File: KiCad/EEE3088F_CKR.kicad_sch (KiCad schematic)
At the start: 0 parts

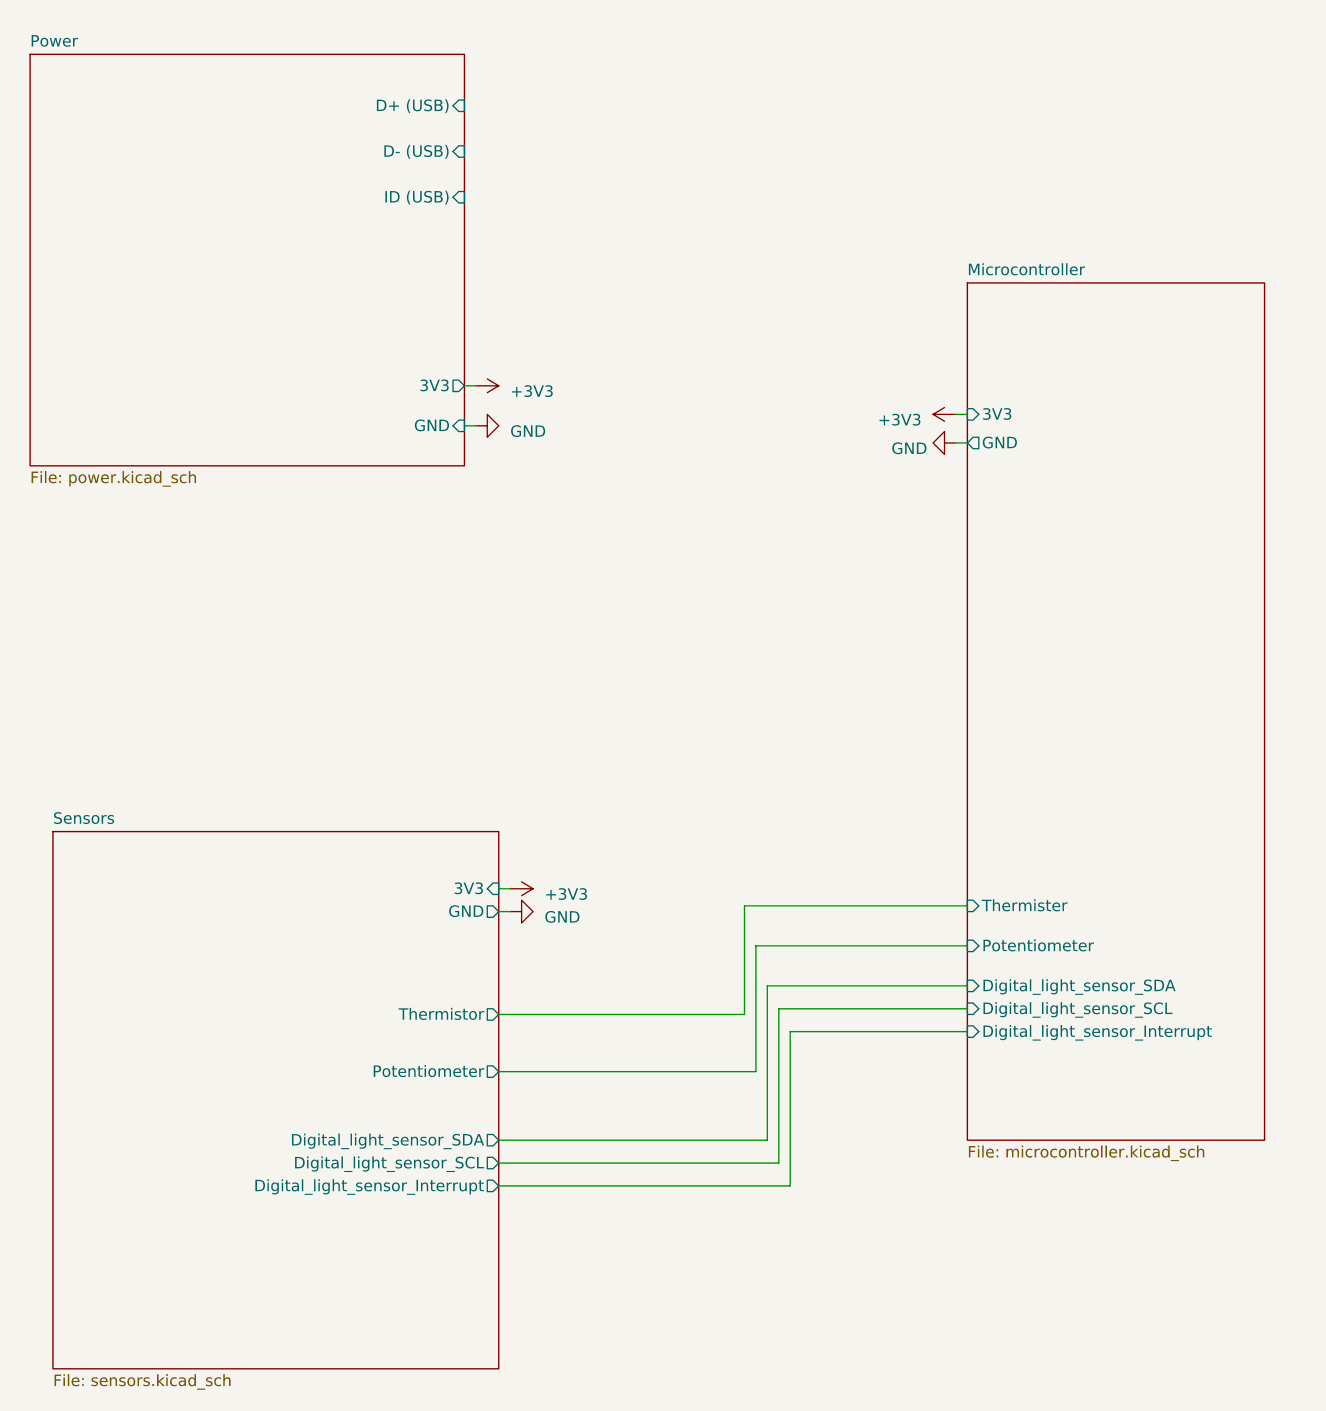
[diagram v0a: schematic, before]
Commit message: added USB to UART connector and made a dedicated USB sheet
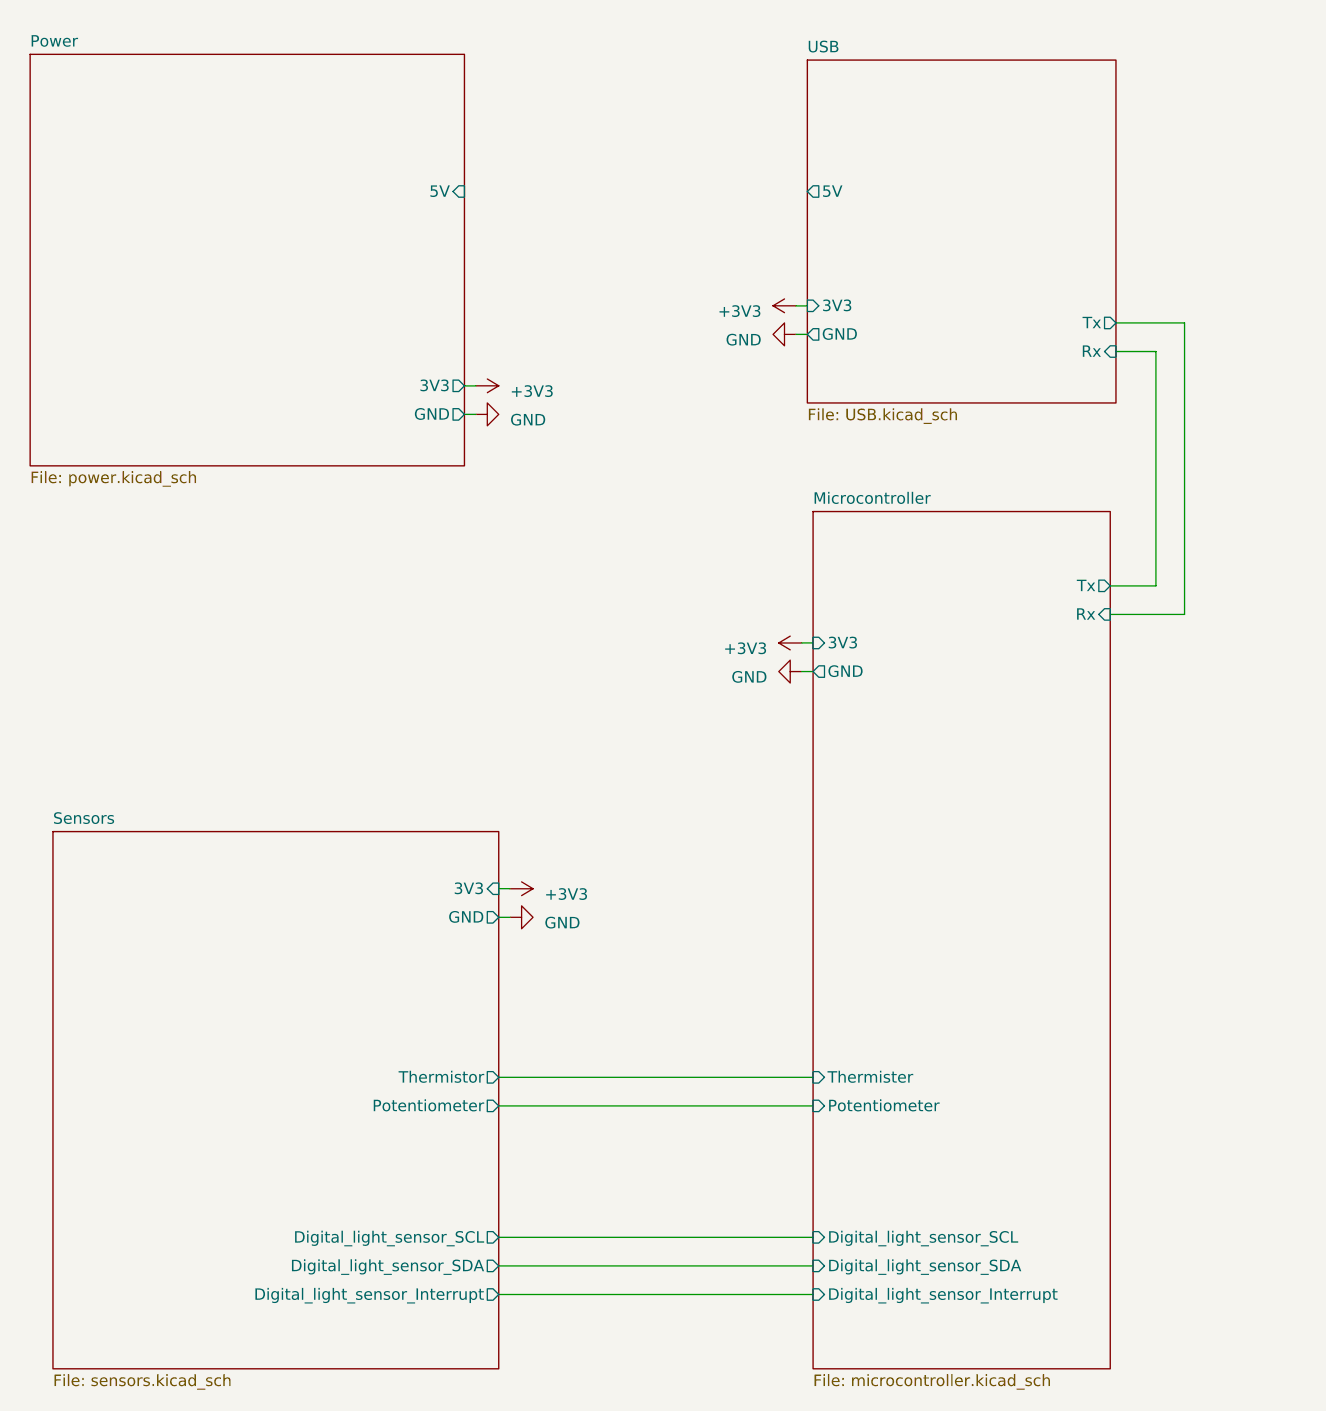
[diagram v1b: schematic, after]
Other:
- added sheet USB (USB.kicad_sch)
- sheet Microcontroller ports: added Rx, Tx; removed none
- sheet Power ports: added 5V; removed D+ (USB), D- (USB), ID (USB)

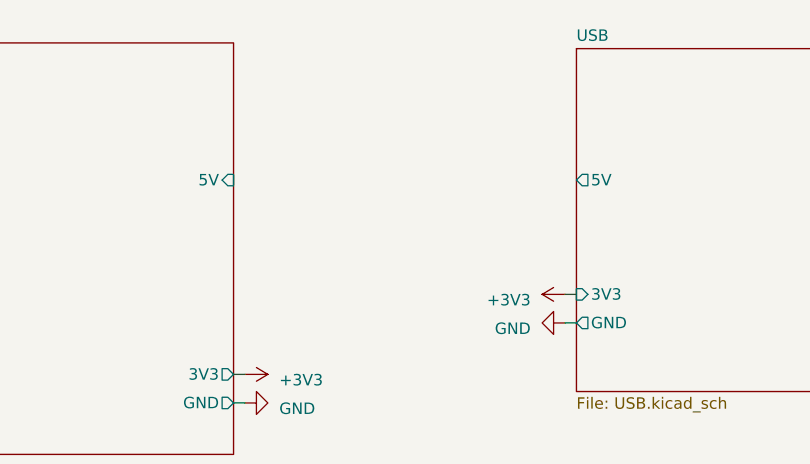
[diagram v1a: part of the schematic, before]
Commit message: Added sheet notes and initial design template, reordered microcontoller subsheet and add microntoller subsheet notes
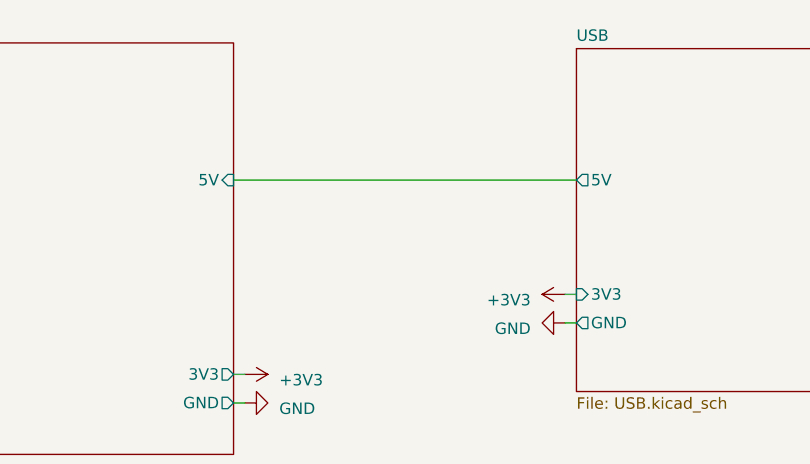
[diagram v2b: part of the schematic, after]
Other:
- company: (none) -> UCT
- title: (none) -> Root
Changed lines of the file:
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@@
 (kicad_sch (version 20230121) (generator eeschema)
   (paper "A4")
+  (title_block
+    (title "Root")
+    (date "2023-03-11")
+    (rev "v0.3")
+    (company "UCT")
+    (comment 1 "Authors: Cameron Clark, Robert Dugmore, Kian Frassek")
+    (comment 2 "This is an overview sheet showing how the sub-circuits interconnect")
+  )
   (wire (pts (xy 118.11 55.88) (xy 116.84 55.88))
     (stroke (width 0) (type default))
@@
     (stroke (width 0) (type default))
   )
+  (wire (pts (xy 80.01 43.18) (xy 118.11 43.18))
+    (stroke (width 0) (type default))
+  )

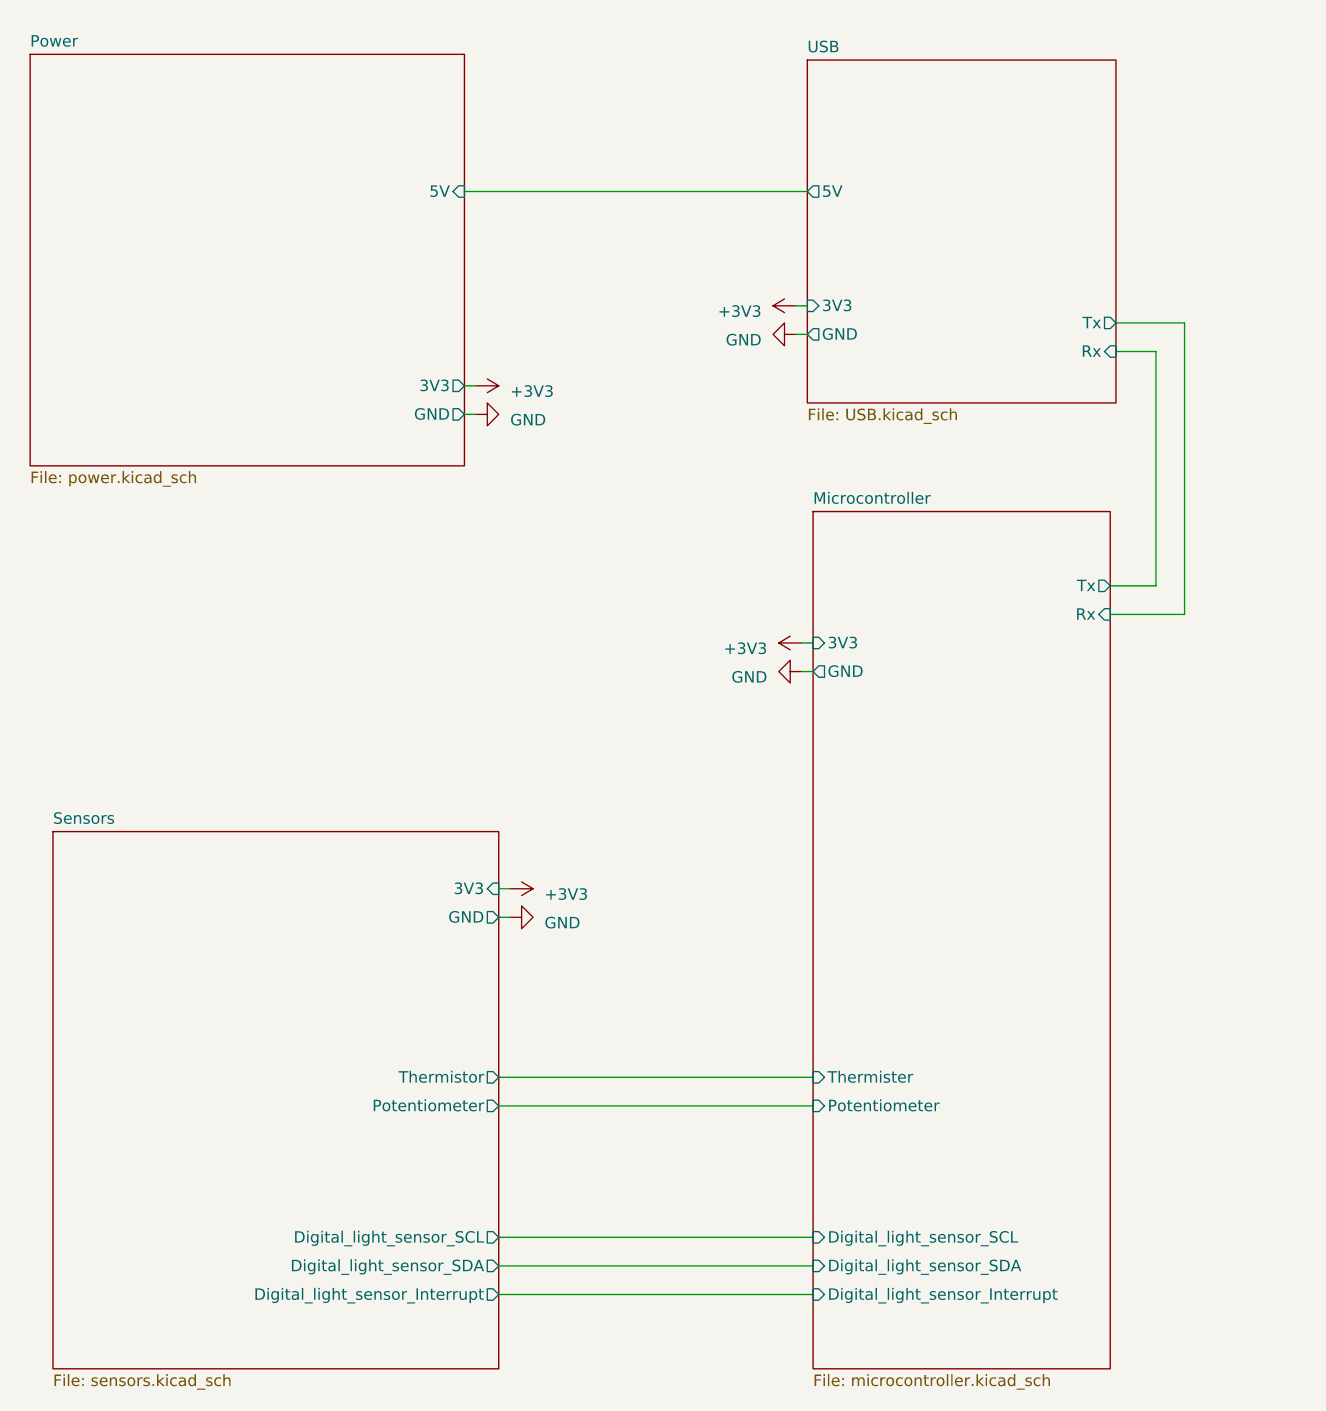
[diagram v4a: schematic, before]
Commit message: updated sensor and microcontroller schematics
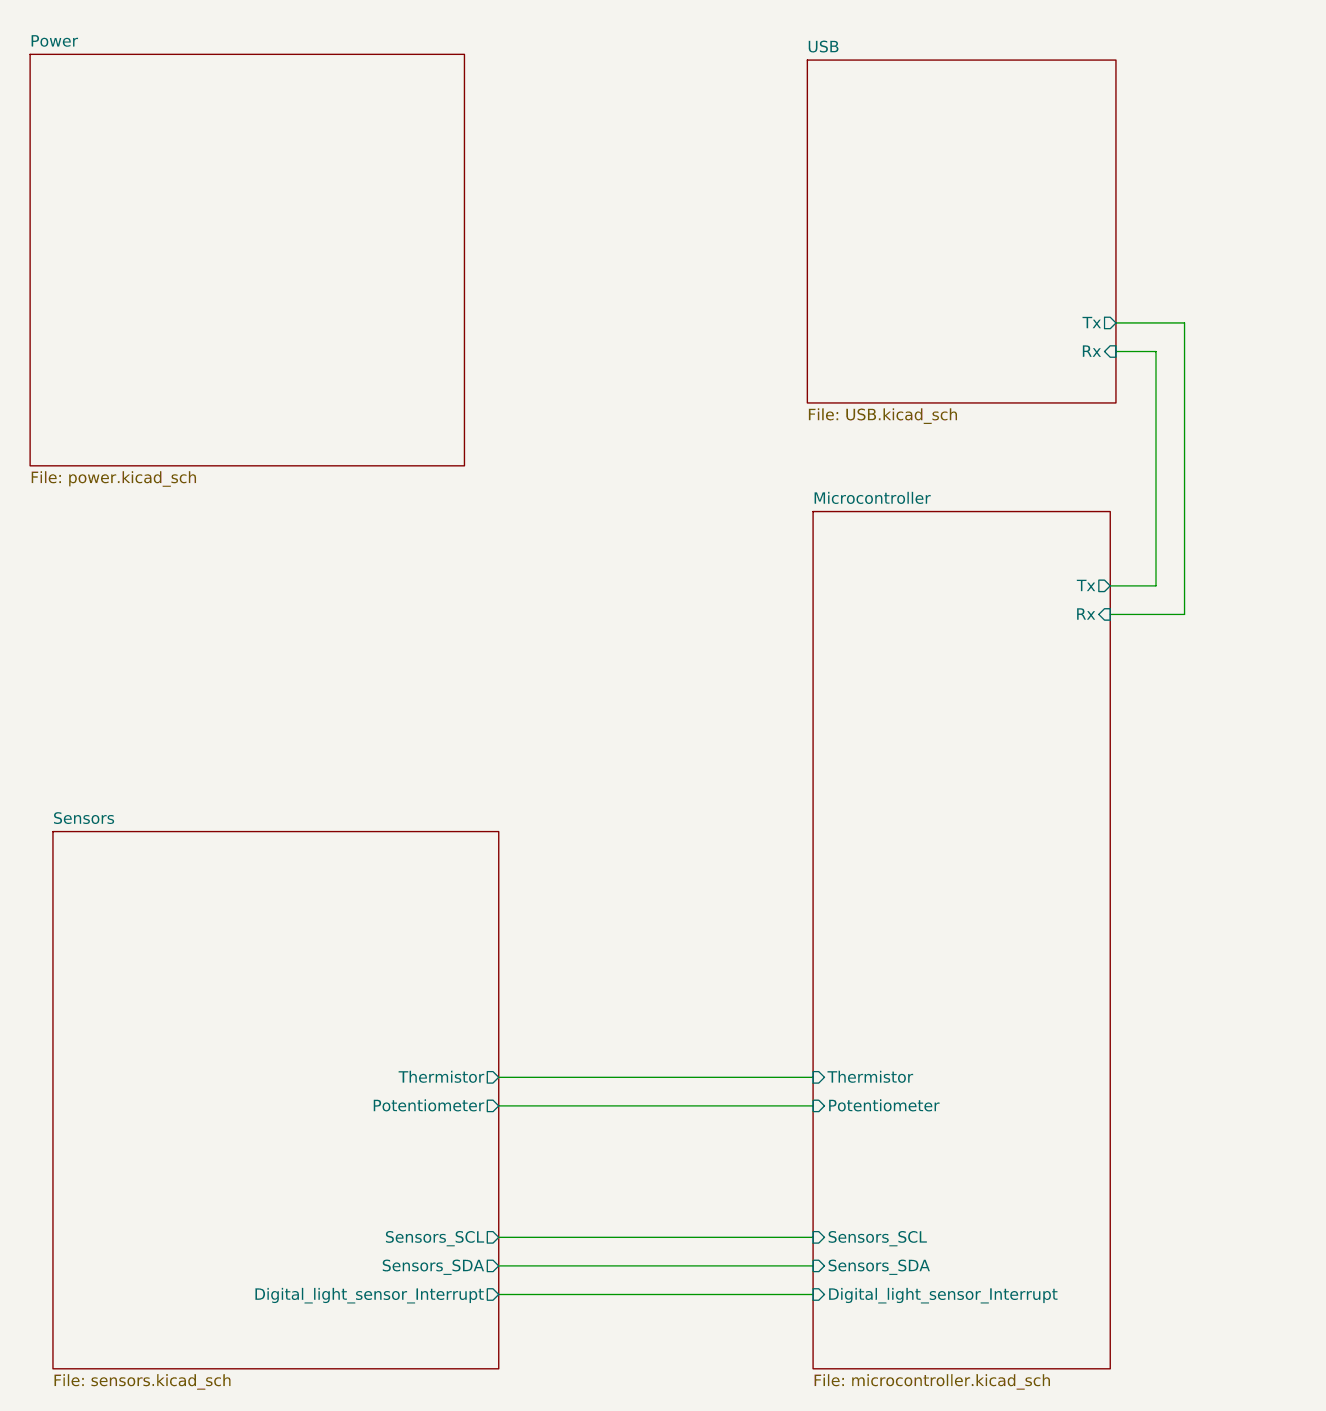
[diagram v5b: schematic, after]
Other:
- sheet Microcontroller ports: added Sensors_SCL, Sensors_SDA, Thermistor; removed 3V3, Digital_light_sensor_SCL, Digital_light_sensor_SDA, GND, Thermister
- sheet Power ports: added none; removed 3V3, 5V, GND
- sheet Sensors ports: added Sensors_SCL, Sensors_SDA; removed 3V3, Digital_light_sensor_SCL, Digital_light_sensor_SDA, GND
- sheet USB ports: added none; removed 3V3, 5V, GND
